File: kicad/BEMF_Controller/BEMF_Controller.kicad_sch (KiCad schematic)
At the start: 75 parts, among them J1 HEADER4VALULOK, J2 HEADER6, J3 FUSE, J7 Vin, Q1 C3M0280090D, Q2 C3M0280090D, Q3 C3M0280090D, Q4 C3M0280090D, Q5 C3M0280090D, Q6 C3M0280090D, U1 Raspberry Pi Pico, U3 V_REG_78XX, U4 TC1240A, U5 DGD2304, U6 DGD2304, U7 DGD2304, U8 ISO7760FQDWRQ1, U9 ISO7760FQDWRQ1

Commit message: Feature complete, zero eroors in pcb. Still lot of warnings.
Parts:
- removed J2: HEADER6, main:6PINVALULOK, symbol main-eagle-import:HEADER6
- removed R1, R2, R3, R4, R5, R6: 2.2k, main:1206, symbol main-eagle-import:RESISTOR1206
- removed U$10, U$11, U$12: SCREW, main:M3HOLE, symbol main-eagle-import:SCREW
- added C59: 22nF, Capacitor_SMD:C_0805_2012Metric, symbol Component_Library:CHV1812N250105MXT
- added C62, C64, C65, C66, C67, C68: 1uF, Capacitor_SMD:C_1812_4532Metric, symbol Component_Library:CHV1812N250105MXT
- added C69, C70: 470uF, main:CPOL-RADIAL-5MM-10MM, symbol main-eagle-import:1000UF-RADIAL-5MM-25V-20%
- added D57, D58, D63: SMD-DIODE-100V-200MA(SOD-123), main:SOD-123, symbol main-eagle-import:SMD-DIODE-100V-200MA(SOD-123)
- added D64: FSV20150V, Package_TO_SOT_SMD:TO-277A, symbol Component_Library:FSV20150V
- added J5: Load, TerminalBlock_Phoenix:TerminalBlock_Phoenix_MKDS-1,5-2-5.08_1x02_P5.08mm_Horizontal, symbol Connector:Conn_01x02_Pin
- added Q11, Q7, Q9: C3M0280090D, Package_TO_SOT_THT:TO-247-3_Horizontal_TabDown, symbol Component_Library:C3M0280090D_TO247
- added R39, R40: 47k, main:1206, symbol main-eagle-import:RESISTOR1206
- added R44, R46, R48: 10, Resistor_THT:R_Axial_DIN0411_L9.9mm_D3.6mm_P15.24mm_Horizontal, symbol Component_Library:ROX1SJ10R
- added U18: ISO7760FQDWRQ1, Package_SO:SOIC-16W_7.5x10.3mm_P1.27mm, symbol Component_Library:ISO7760FQDWRQ1
- added U19, U20, U21: DGD2304, main:SOIC8, symbol main-eagle-import:DGD2304
- Q1, Q2, Q3, Q4, Q5, Q6: footprint main:TO-247-3_Horizontal_TabDown-with-pad -> Package_TO_SOT_THT:TO-247-3_Horizontal_TabDown
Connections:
- net 10V: now also D57.+, D58.+, D63.+, U19.3 (VCC), U20.3 (VCC), U21.3 (VCC)
- net 3.3V: now also C62.1, U18.1 (Vcc1)
- net 5V: now also C64.1, U18.16 (Vcc2)
- net CAP_BANK_A+: now also Q7.2 (D); no longer Q2.4 (D)
- net CAP_BANK_B+: now also Q9.2 (D); no longer Q3.4 (D)
- net CAP_BANK_C+: now also Q11.2 (D); no longer Q5.4 (D)
- net COIL_A_-: no longer Q1.4 (D)
- net COIL_B_-: no longer Q4.4 (D)
- net COIL_C_-: no longer Q6.4 (D)
- net GND: now also C62.2, C64.2, C68.2, C69.-, C70.-, J5.2 (Pin_2), U18.8 (GND1), U18.9 (GND2), U19.4 (GND), U20.4 (GND), U21.4 (GND)
- net GNDA: now also C59.2, R40.1
- net THROTTLE: no longer U1.34 (GPIO28_ADC2)
- net V_RAW: now also D64.1 (A), D64.2 (A)
- net at J1.1: now also R39.1
- net DA_O: now reaches U1.14 (GPIO10)
- net DA_O: now also U18.2 (INA)
- net DB_O: now reaches U1.15 (GPIO11)
- net DB_O: now also U18.3 (INB)
- net DC_O: now reaches U1.16 (GPIO12)
- net DC_O: now also U18.4 (INC)
- net ISENSE renamed ISENSE_A_HALL_1
- net VSENSE renamed ISENSE_B_HALL_2
- new net: C65.1, D57.-, U19.8 (VB)
- new net: Q7.1 (G), R44.1
- new net: C67.1, D63.-, U21.8 (VB)
- new net: C66.1, D58.-, U20.8 (VB)
- new net: Q11.1 (G), R48.1
- new net: Q9.1 (G), R46.1
- new net CTRL_DA: U18.15 (OUTA), U19.2 (HIN)
- new net CTRL_DB: U18.14 (OUTB), U20.2 (HIN)
- new net CTRL_DC: U18.13 (OUTC), U21.2 (HIN)
- new net DCH_A_H: R44.2, U19.7 (HO)
- new net DCH_B_H: R46.2, U20.7 (HO)
- new net DCH_C_H: R48.2, U21.7 (HO)
- new net DUTY: C59.1, R39.2, R40.2
- new net ISENSE_C_HALL_3: U1.34 (GPIO28_ADC2)
- new net LOAD+: C65.2, C66.2, C67.2, C68.1, C69.+, C70.+, D64.3 (K), J5.1 (Pin_1), Q11.3 (S), Q7.3 (S), Q9.3 (S), U19.6 (VS), U20.6 (VS), U21.6 (VS)
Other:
- added sheet Hall Inputs (Hall_Inputs.kicad_sch)
- note added: "Digital isolators"
- note added: "Discharge to load"
- note added: "Throttle/Freq and Duty"
- note removed: "Hall Input"
- note removed: "Throttle"
- moved on the sheet: C1, C11, C12, C14, C15, C16, C18, C19, C2, C20, C3, C4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

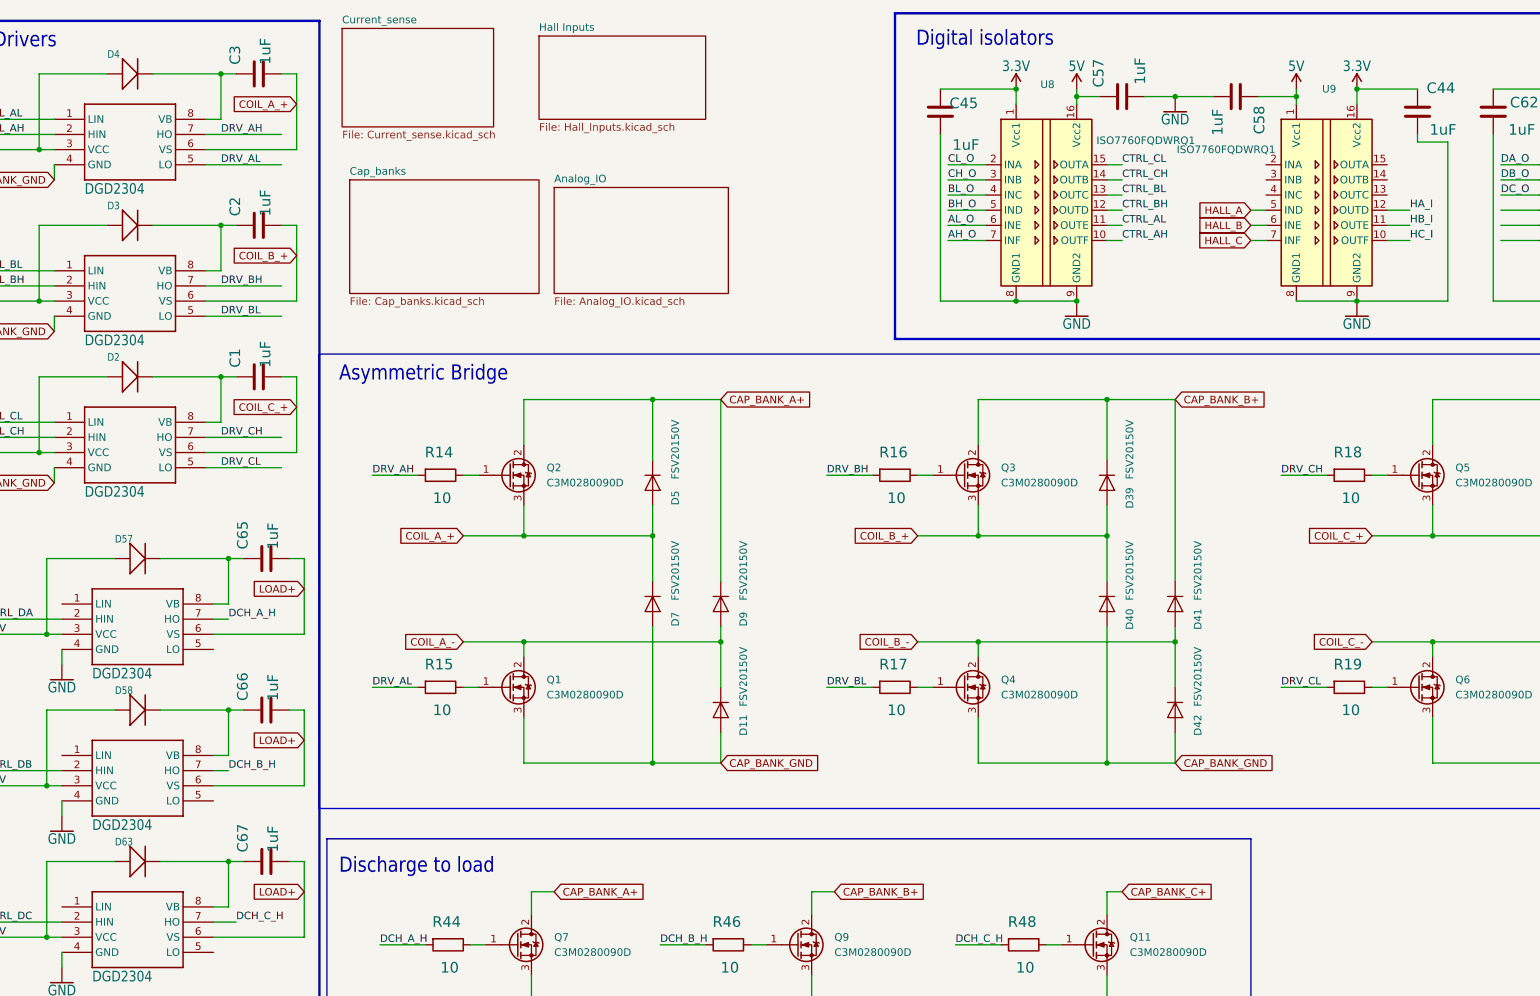
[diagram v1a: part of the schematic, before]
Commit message: Added analog Hall inputs and worked away lot of warnings.
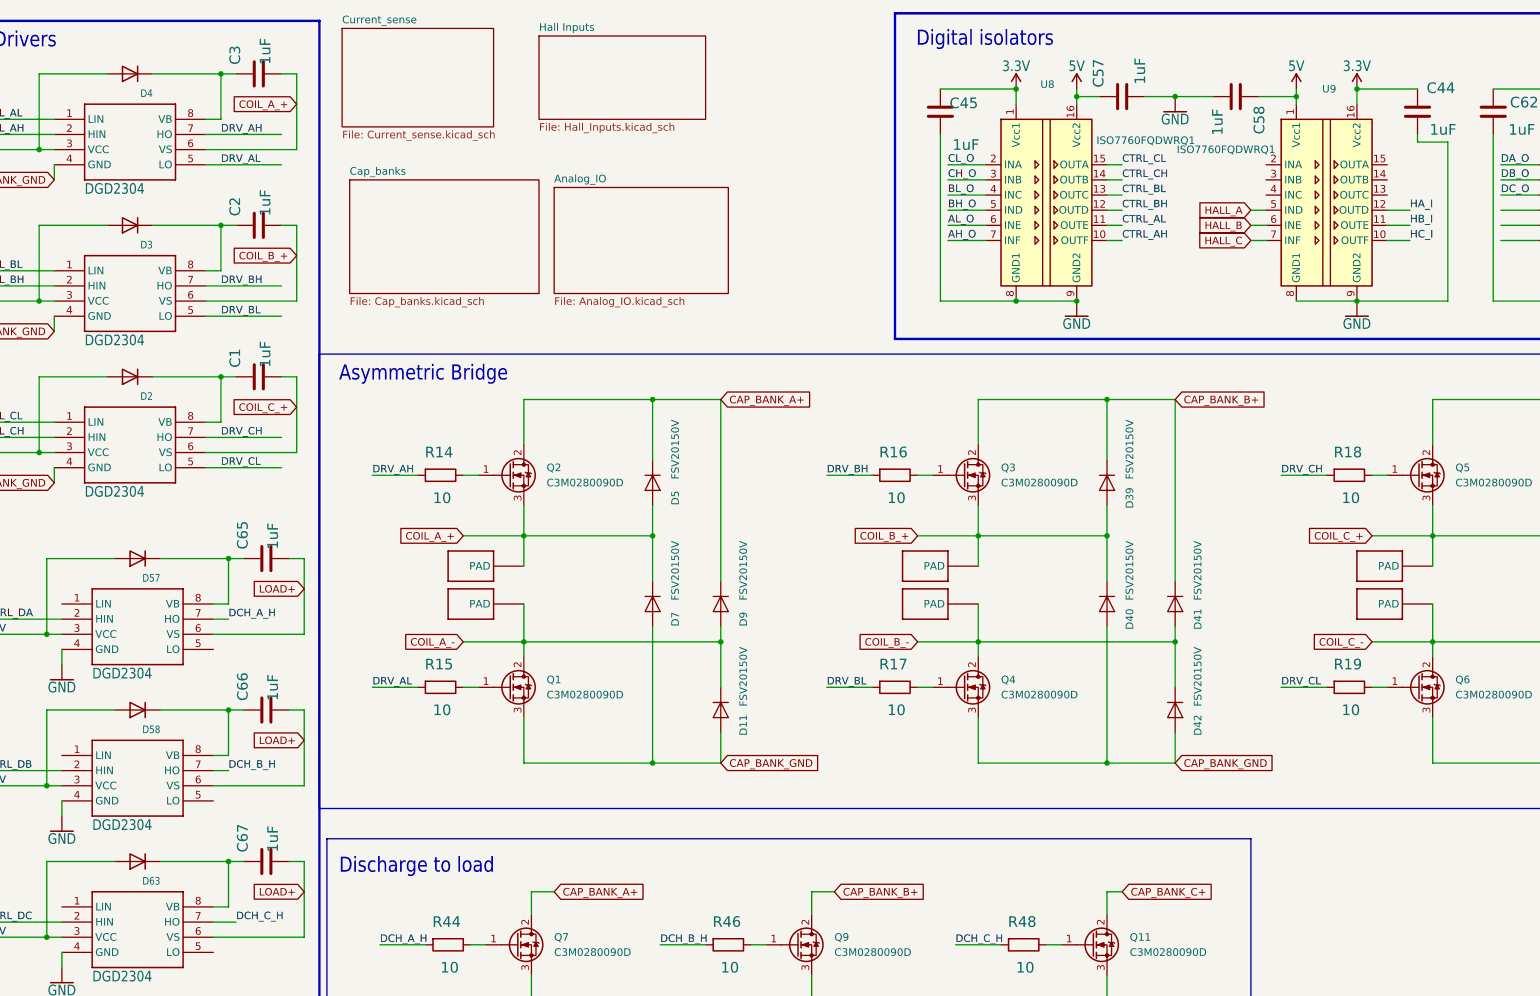
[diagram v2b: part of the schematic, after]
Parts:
- added U$1, U$2, U$3, U$6, U$7, U$8: PAD, main:PAD, symbol main-eagle-import:PAD
- D2, D3, D4, D57, D58, D63: footprint main:SOD-123 -> Diode_SMD:D_SOD-123; symbol main-eagle-import:SMD-DIODE-100V-200MA(SOD-123) -> Component_Library:SMD110PL-TP
- U19, U20, U21, U5, U6, U7: footprint main:SOIC8 -> Package_SO:SOIC-8_3.9x4.9mm_P1.27mm; symbol main-eagle-import:DGD2304 -> Component_Library:DGD2304
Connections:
- net 10V: now also D2.2 (A), D3.2 (A), D4.2 (A), D57.2 (A), D58.2 (A), D63.2 (A); no longer D2.+, D3.+, D4.+, D57.+, D58.+, D63.+
- net COIL_A_+: now also U$1.PAD
- net COIL_A_-: now also U$2.PAD
- net COIL_B_+: now also U$3.PAD
- net COIL_B_-: now also U$6.PAD
- net COIL_C_+: now also U$7.PAD
- net COIL_C_-: now also U$8.PAD
- net at C2.1, U6.8 (VB): now also D3.1 (K); no longer D3.-
- net at C65.1, U19.8 (VB): now also D57.1 (K); no longer D57.-
- net at C1.1, U7.8 (VB): now also D2.1 (K); no longer D2.-
- net at C67.1, U21.8 (VB): now also D63.1 (K); no longer D63.-
- net at C66.1, U20.8 (VB): now also D58.1 (K); no longer D58.-
- net at C3.1, U5.8 (VB): now also D4.1 (K); no longer D4.-

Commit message: Simplification, high and low side driven together.
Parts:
- removed C62, C64: 1uF, Capacitor_SMD:C_1812_4532Metric, symbol Component_Library:CHV1812N250105MXT
- removed U18: ISO7760FQDWRQ1, Package_SO:SOIC-16W_7.5x10.3mm_P1.27mm, symbol Component_Library:ISO7760FQDWRQ1
- C4, C5, C69, C70: footprint main:CPOL-RADIAL-5MM-10MM -> Capacitor_THT:CP_Radial_D10.0mm_P5.00mm; symbol main-eagle-import:1000UF-RADIAL-5MM-25V-20% -> Component_Library:C_Pol_470uF
- U$1: value PAD -> COIL_A+
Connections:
- net BL_O is gone; now on net DA_O: U1.25 (GPIO19), U8.4 (INC)
- net CH_O is gone; now on net DB_O: U1.26 (GPIO20), U8.3 (INB)
- net CL_O is gone; now on net DC_O: U1.27 (GPIO21), U8.2 (INA)
- net CTRL_DA: now also U8.13 (OUTC)
- net CTRL_DB: now also U8.14 (OUTB)
- net CTRL_DC: now also U8.15 (OUTA)
- net DA_O: no longer U1.14 (GPIO10)
- net DB_O: no longer U1.15 (GPIO11)
- net DC_O: no longer U1.16 (GPIO12)
- net GND: now also C4.2, C5.2, C69.2, C70.2, U1.42 (GND); no longer C4.-, C5.-, C69.-, C70.-
- net LOAD+: now also C69.1, C70.1; no longer C69.+, C70.+
- net V_RAW: now also C4.1, C5.1; no longer C4.+, C5.+
- net AH_O renamed A_O
- net AL_O renamed B_O
- net BH_O renamed C_O
- net CTRL_AH renamed CTRL_A
- net CTRL_A: now also U5.1 (LIN)
- net CTRL_AL renamed CTRL_B
- net CTRL_B: now also U6.1 (LIN), U6.2 (HIN); no longer U5.1 (LIN)
- net CTRL_BH renamed CTRL_C
- net CTRL_C: now also U7.1 (LIN), U7.2 (HIN); no longer U6.2 (HIN)
- removed net CTRL_BL: U6.1 (LIN), U8.13 (OUTC)
- removed net CTRL_CH: U7.2 (HIN), U8.14 (OUTB)
- removed net CTRL_CL: U7.1 (LIN), U8.15 (OUTA)
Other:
- moved on the sheet: C11, C14, C15, C16, C18, C19, C20, C44, C45, C68, D64, J5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

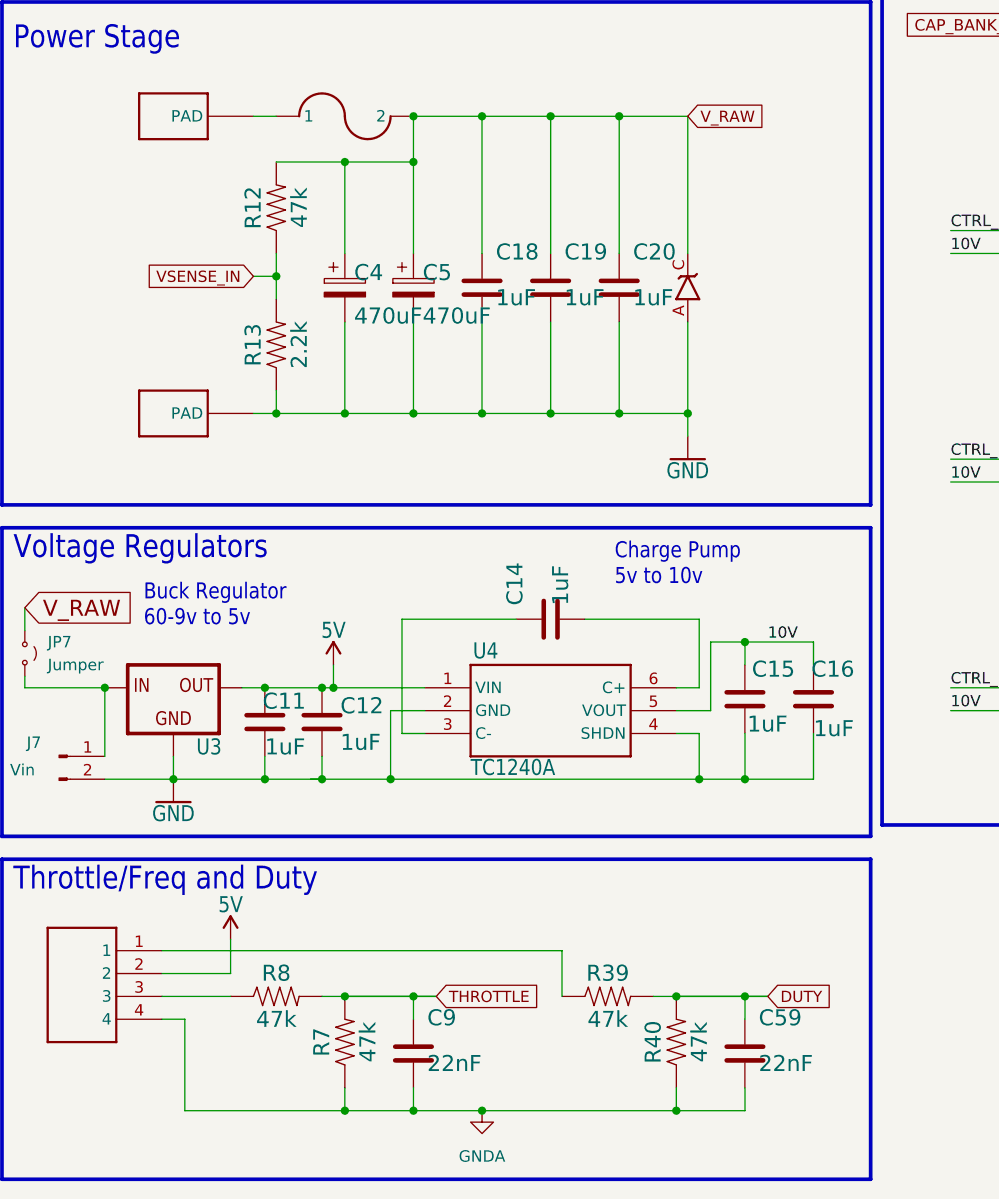
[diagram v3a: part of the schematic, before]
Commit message: Fixed all warnings.
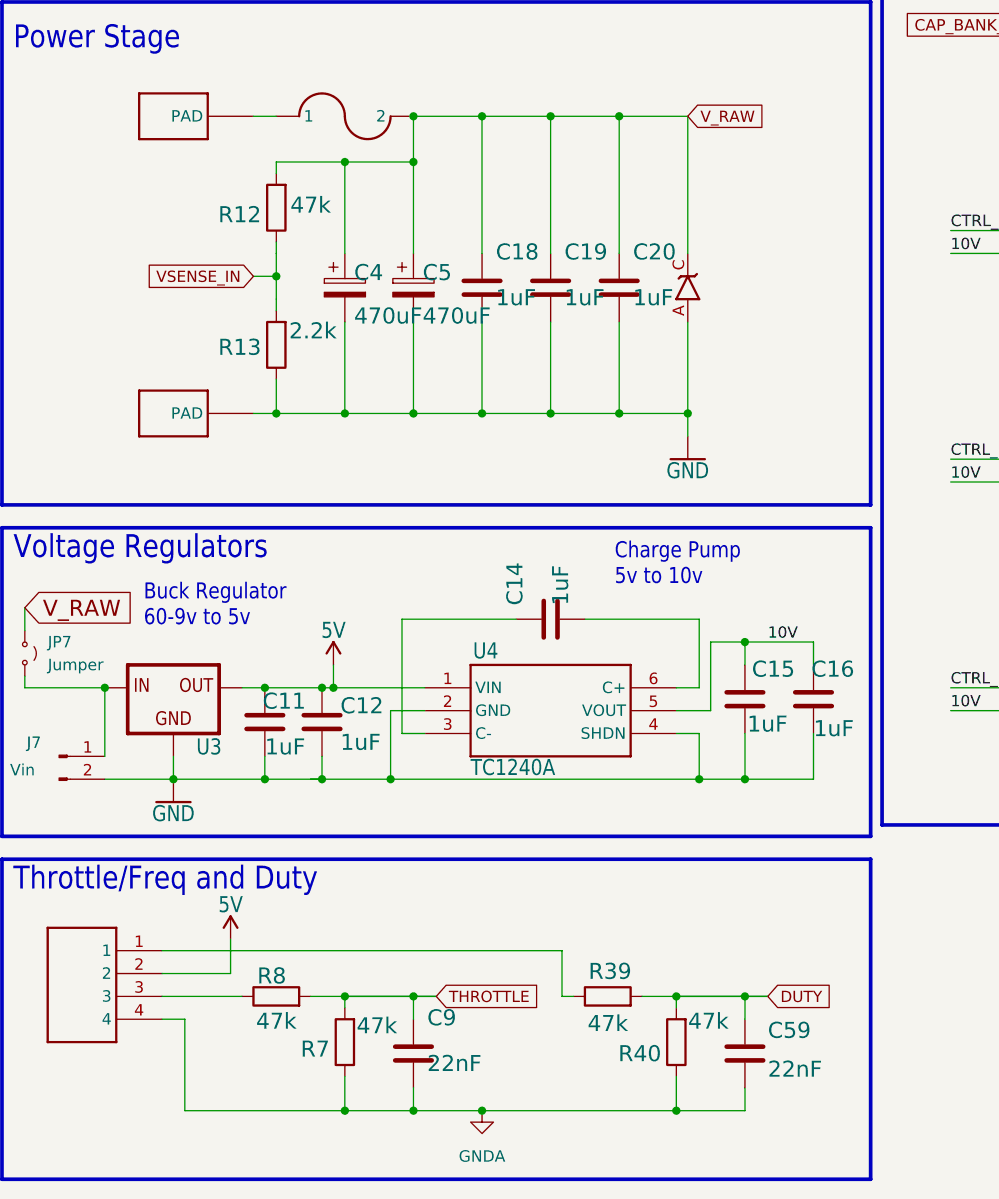
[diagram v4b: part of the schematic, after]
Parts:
- R12, R39, R40, R7, R8: footprint main:1206 -> Resistor_SMD:R_1206_3216Metric; symbol main-eagle-import:RESISTOR1206 -> Component_Library:R47k
- R13: footprint main:1206 -> Resistor_SMD:R_1206_3216Metric; symbol main-eagle-import:RESISTOR1206 -> Component_Library:R2k2
